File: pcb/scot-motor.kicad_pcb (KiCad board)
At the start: 2 copper layers, 115.1 x 80.1 mm, 86 parts, among them IC1 MCP2562, IC2 STM32F0xxKxTx, IC3 NCV8450A, J1 Conn_01x03_Female, J2 Conn_01x03_Female, J3 Conn_01x02_Female, J4 Conn_01x03_Female, J5 Conn_01x02_Female, J6 Conn_01x02_Female, J7 Conn_01x02_Female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

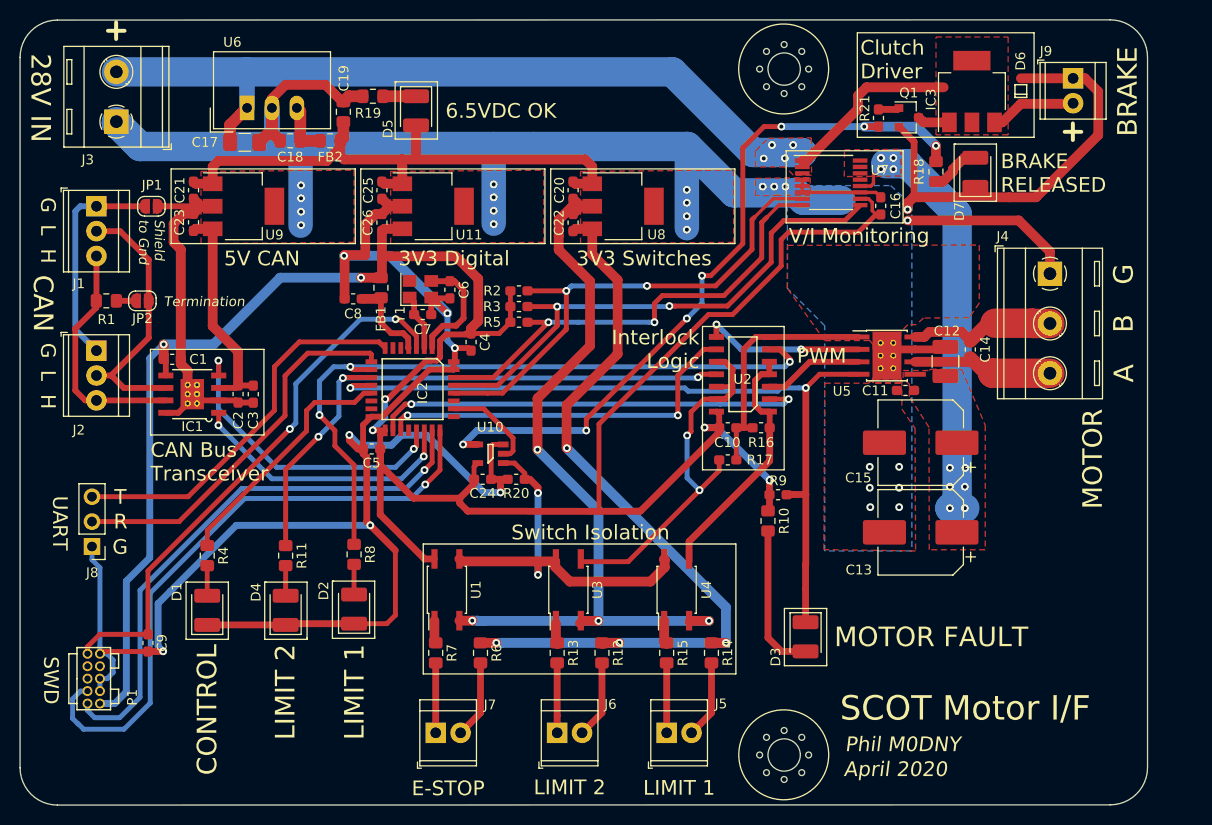
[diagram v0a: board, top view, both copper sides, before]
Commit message: pcb: Fix some DRC warnings, produce gerbers for cam.
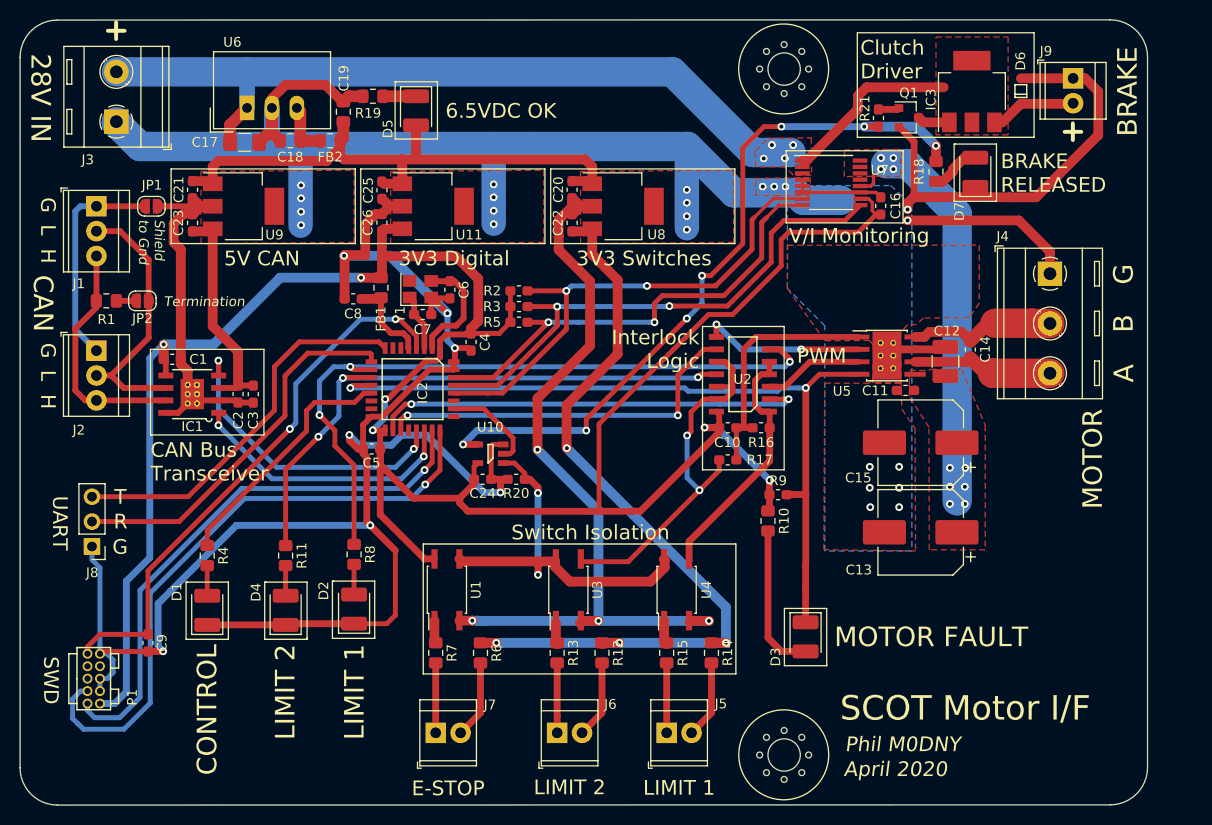
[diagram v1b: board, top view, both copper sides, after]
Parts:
- moved C20 0.11 mm to (121.4, 60.3)
- moved C23 0.11 mm to (82.6, 63.7)
- moved C21 0.11 mm to (82.6, 60.3)
- moved C22 0.10 mm to (121.4, 63.7)
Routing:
- net GND: track 540.1 -> 544.4 mm
- net /Power Supplies/MOTOR_28V+: track 45.3 -> 42.7 mm
- net /MCU/POWER_28V+: track 100.5 -> 99.4 mm

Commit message: pcb/: Fixi C3 footprint and re-plot.
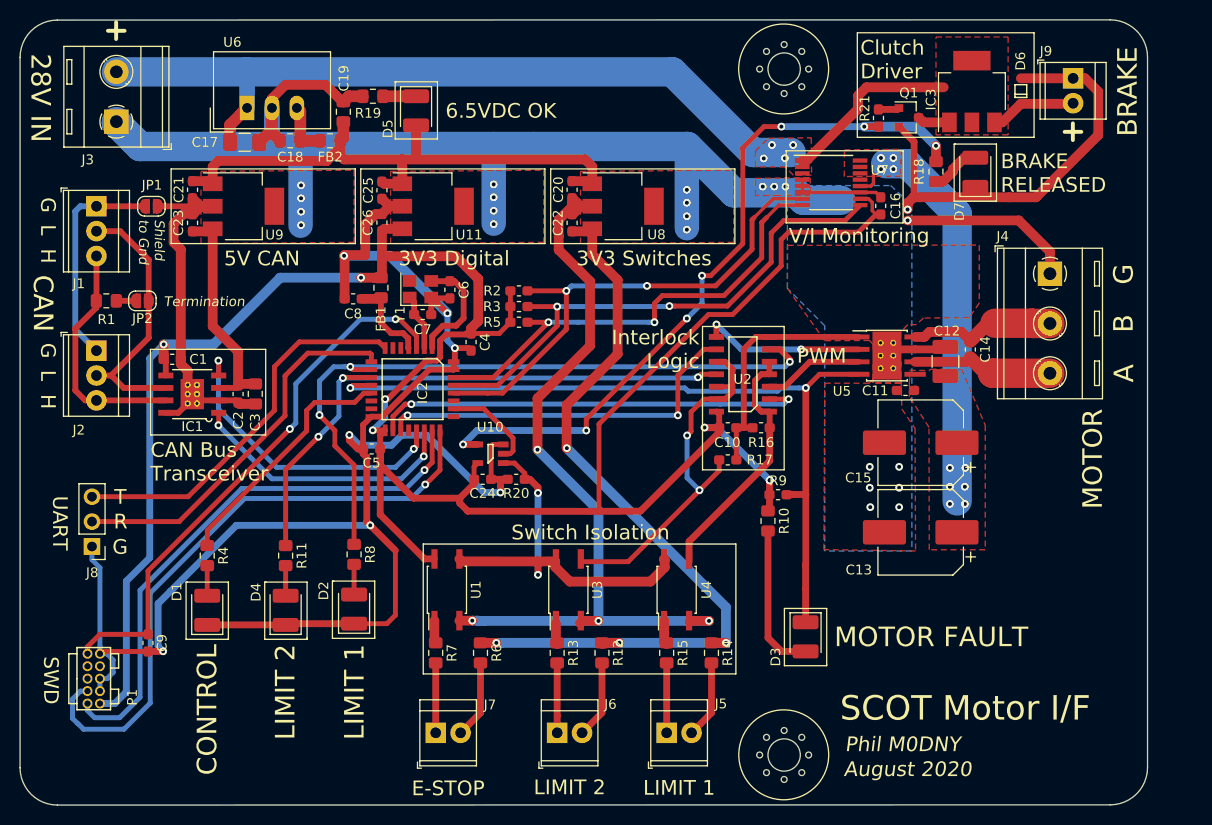
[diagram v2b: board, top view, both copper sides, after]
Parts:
- C13, C15: value 22u/50V -> 33u/50V
- C19: value 10u/6.5V -> 4u7/6.5V
- C3: value 1u/5V -> 4u7/5V; footprint Capacitor_SMD:C_0603_1608Metric_Pad1.05x0.95mm_HandSolder -> Capacitor_SMD:C_0805_2012Metric_Pad1.15x1.40mm_HandSolder
- C6, C7: value 12p -> 8p
- FB1, FB2: value Ferrite_Bead_Small -> 600R@100M/1A
- R19: value R -> 180R
- moved C3 0.20 mm to (89.0, 81.2)
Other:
- board text added: "August 2020"
- board text removed: "April 2020"
